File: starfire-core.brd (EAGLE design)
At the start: 60 x 52 mm, 70 parts, among them Q1 FDN340P, Y1 16MHZ

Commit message: starfire eaglecad lbr refernce moved.
I renamed and moved the EagleCAD library for the PCB fab compoment to our public git repo.  So updated the BRD and SCH references so that users can find the correct library.
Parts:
- FAB: device CircuitMonkey-solaris:PCB-BASE-B1 -> solstice-design-system:PCB-BASE-B1
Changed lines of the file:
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@@
 <attribute name="VALUE" x="-24.5" y="23" size="0.6096" layer="27" font="vector" align="center"/>
 </element>
-<element name="FAB" library="CircuitMonkey-solaris" package="PCB-BASE-B1" value="STARFIRE PCB" x="0" y="0" smashed="yes"/>
+<element name="FAB" library="solstice-design-system" package="PCB-BASE-B1" value="STARFIRE PCB" x="0" y="0" smashed="yes"/>
 <element name="OPAMP" library="Seeed-IC" package="MSOP8-0.65-3X3MM" value="LMV358IDGKR-MSOP8" x="-15" y="-3.3048" smashed="yes">
 <attribute name="MPN" value="LMV358IDGKR" x="-15" y="-3.3048" size="1.778" layer="27" display="off"/>

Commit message: Rev. A PCBs shared to world
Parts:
- removed WS1, WS10, WS11, WS12, WS13, WS14, WS15, WS16, WS2, WS3, WS4, WS5, WS6, WS7, WS8, WS9: WS2812, led:NEOPIXEL
- added C17, C18: 10uf, Seeed-Capacitor:C0603
- added SK0, SK1, SK10, SK11, SK12, SK13, SK14, SK15, SK2, SK3, SK4, SK5, SK6, SK7, SK8, SK9: SK6812-MINI, led:SMD_3535
- added UMBRA: DF12-20DS-0.5V, co-hirose:DF12-20P-RCPT-MTL-BOSS
- added US0, US1, US2: TPSMD-040-RND, con-testpoints:SMD-040MIL-RND
- RESET: value B3U-1000P-2P-SMD -> MOM (OFF)-ON; device Seeed-Switch:SW2-2.6-3.0X2.5X1.2+0.4MM -> comp-switch:SWITCH-0635-2P-SMD
- VR33: value XC6206P332MR-G-SOT23 -> 3.3V
- moved RESET 77.9 mm to (27.5, 42.6), turned to 0 degrees
- moved C8 40.7 mm to (34.5, 16.6), turned to 90 degrees
- moved C16 39.2 mm to (16.7, 23.1), turned to 270 degrees
- moved 5-12V 39.0 mm to (0.10, 34.0)
- moved USB 38.5 mm to (1.50, 24.0)
- moved C1 38.4 mm to (33.0, 31.6)
- moved C10 38.4 mm to (15.0, 28.2)
- moved C11 38.4 mm to (15.0, 26.8)
- moved C12 38.4 mm to (21.0, 22.6)
- moved C13 38.4 mm to (12.0, 36.8)
- moved C14 38.4 mm to (23.9, 34.4)
- moved C15 38.4 mm to (21.0, 18.4)
- moved C2 38.4 mm to (21.0, 25.2)
- moved C3 38.4 mm to (21.0, 19.8)
- moved C4 38.4 mm to (33.0, 30.2)
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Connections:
- removed net MOSI/WS2812: ICSP.5, R8.1, UC.10
- removed net N$29: WS11.2, WS12.4
- removed net N$30: WS12.2, WS13.4
- removed net N$31: WS13.2, WS14.4
- removed net N$32: WS14.2, WS15.4
- removed net N$33: WS15.2, WS16.4
- removed net PIXELS: R8.2, WS1.4
- removed net SCK: ICSP.2, UC.9
- new net MOSI: ICSP.5, UC.10, UMBRA.16
- new net N$1: SK0.1, SK1.3
- new net N$12: SK6.1, SK7.3
- new net N$4: SK1.1, SK2.3
- new net N$5: SK2.1, SK3.3
- new net N$6: SK3.1, SK4.3
- new net N$9: SK4.1, SK5.3
- new net SCK/PIXELS: ICSP.2, R8.1, UC.9, UMBRA.12
- new net SL0: UMBRA.2, US0.TP
- new net SL1: UMBRA.4, US1.TP
- new net SL2: UMBRA.6, US2.TP
- net !RESET: now also RESET.1, UMBRA.10; no longer RESET.2
- net +3V3: now also UMBRA.8
- net D0: now also UMBRA.15
- net D1: now also UMBRA.13
- net D2: now also UMBRA.11
- net D3: now also UMBRA.9
- net D4: now also UMBRA.7
- net D5: now also UMBRA.5
- net D6: now also UMBRA.3
- net D7: now also UMBRA.1
- net GND: now also C17.1, C18.1, HL4.1, RESET.2, SK0.2, SK1.2, SK10.2, SK11.2, SK12.2, SK13.2, SK14.2, SK15.2, SK2.2, SK3.2, SK4.2, SK5.2, SK6.2, SK7.2, SK8.2, SK9.2, UMBRA.19, UMBRA.20; no longer HL4.2, RESET.1, WS1.3, WS10.3, WS11.3, WS12.3, WS13.3, WS14.3, WS15.3, WS16.3, WS2.3, WS3.3, WS4.3, WS5.3, WS6.3, WS7.3, WS8.3, WS9.3
- net MISO: now also UMBRA.14
- net N$11: now also SK5.1, SK6.3; no longer WS1.2, WS2.4
- net N$13: now also SK8.1, SK9.3; no longer WS2.2, WS3.4
- net N$14: now also R8.2, SK0.3; no longer WS3.2, WS4.4
- net N$15: now also SK10.3, SK9.1; no longer WS4.2, WS5.4
- net N$16: now also SK10.1, SK11.3; no longer WS5.2, WS6.4
- net N$17: now also SK11.1, SK12.3; no longer WS6.2, WS7.4
- net N$18: now also SK12.1, SK13.3; no longer WS7.2, WS8.4
- net N$19: now also SK13.1, SK14.3; no longer WS8.2, WS9.4
- net N$20: now also SK14.1, SK15.3; no longer WS10.4, WS9.2
- net N$28: now also SK7.1, SK8.3; no longer WS10.2, WS11.4
- net VCC: now also C17.2, C18.2, SK0.4, SK1.4, SK10.4, SK11.4, SK12.4, SK13.4, SK14.4, SK15.4, SK2.4, SK3.4, SK4.4, SK5.4, SK6.4, SK7.4, SK8.4, SK9.4, UMBRA.17, UMBRA.18; no longer WS1.1, WS10.1, WS11.1, WS12.1, WS13.1, WS14.1, WS15.1, WS16.1, WS2.1, WS3.1, WS4.1, WS5.1, WS6.1, WS7.1, WS8.1, WS9.1
- net VIN: now also HL4.2; no longer HL4.1
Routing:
- net SCK/PIXELS: track 0.00 -> 60.3 mm, vias 0 -> 2
- net N$28: track 4.32 -> 59.0 mm, vias 0 -> 2
- net MOSI: track 0.00 -> 54.1 mm, vias 0 -> 2
- net N$19: track 53.3 -> 4.32 mm, vias 2 -> 0
- net N$14: track 4.32 -> 43.9 mm, vias 0 -> 2
- net D7: track 23.8 -> 63.3 mm
- net MOSI/WS2812: track 35.1 -> 0.00 mm, vias 2 -> 0
- net D4: track 31.0 -> 58.5 mm
- net +3V3: track 42.0 -> 69.4 mm, vias 3 -> 4
- net D6: track 29.6 -> 55.9 mm, vias 0 -> 2
- net SCK: track 25.9 -> 0.00 mm, vias 2 -> 0
- net D5: track 35.6 -> 60.5 mm
- net D3: track 32.7 -> 57.5 mm
- net D2: track 34.5 -> 58.5 mm
- net D1: track 33.6 -> 56.5 mm
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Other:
- board size 60 x 52 mm -> 60 x 48 mm
- board text added: "Rev. A"
- board text removed: "Rev. *"

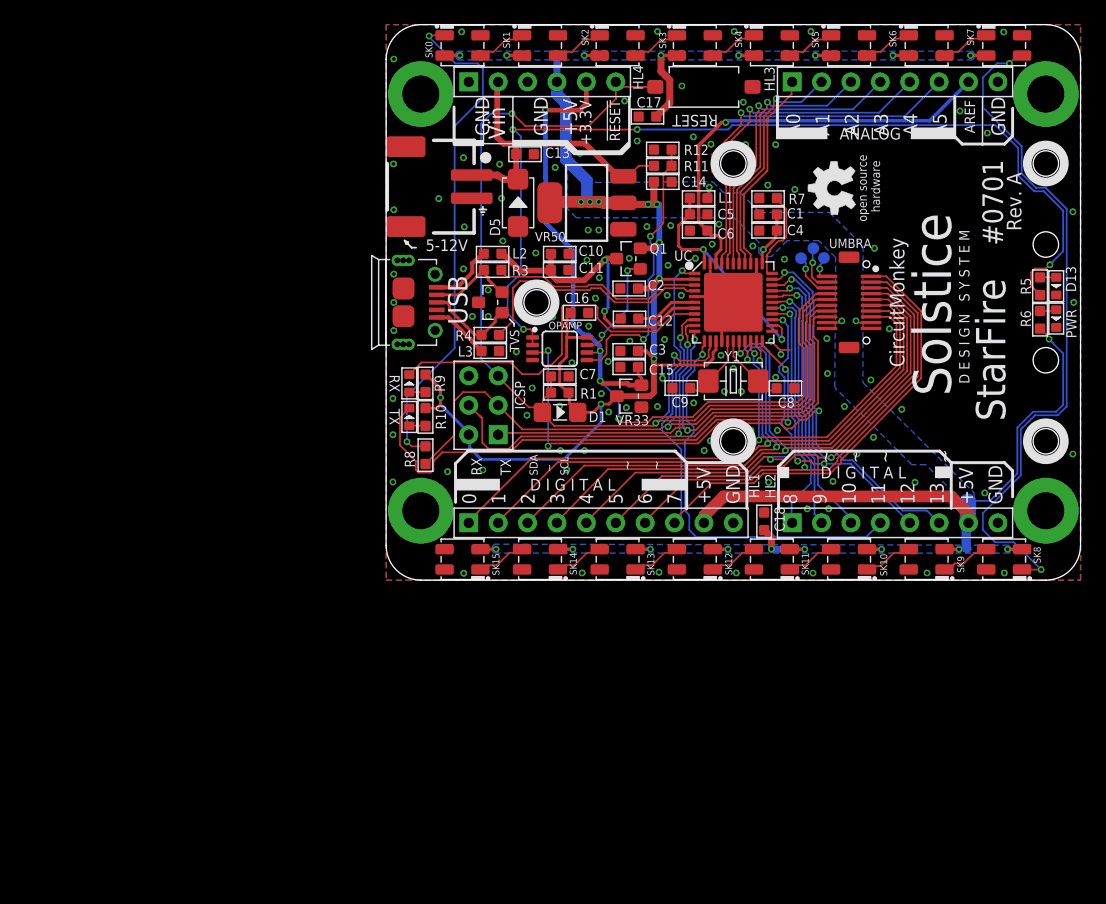
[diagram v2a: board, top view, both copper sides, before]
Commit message: Revision B released
Added Umbra connector feature along with Umbra mount support holes.  RGB LEDs are now smaller SK6812 type 3.5x3.5mm.   Added output test points for external LED chain that extends on-board chain.  Added PIXEL_EN solder jumper so that user can disable on board pixels if needed.
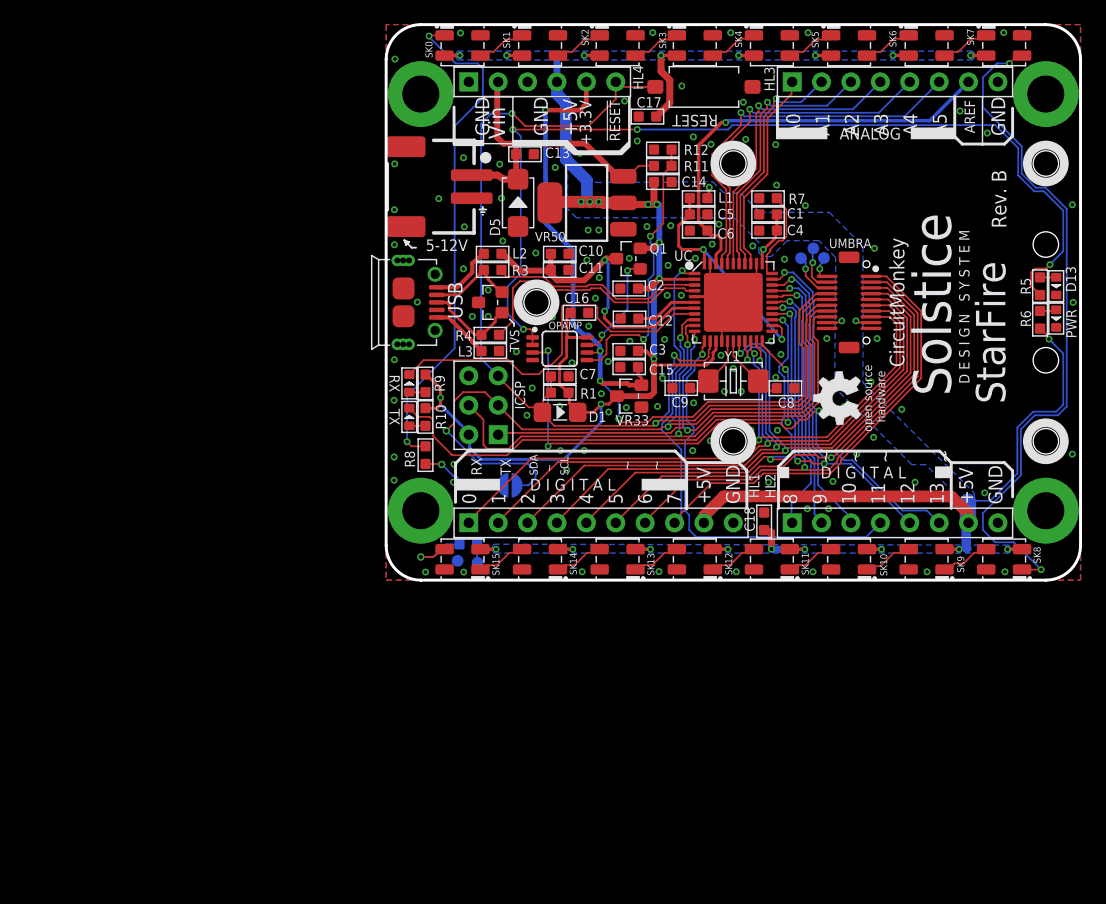
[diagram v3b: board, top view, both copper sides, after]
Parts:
- added EN_PIXELS: (no value), rlc:SOLDER_JUMP_80MIL_RND
- added PXGND, PXO: TPSMD-040-RND, con-testpoints:SMD-040MIL-RND
- added R2: 330R, Seeed-Resistor:R0603
- USB: value ZX62-B-5PA -> USB-Micro-SMT+THD
- moved U$3 43.4 mm to (47.2, 14.5)
- moved U$2 18.2 mm to (39.2, 15.7)
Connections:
- new net N$29: PXO.TP, R2.1
- new net N$30: R2.2, SK15.1
- new net PIXELS: EN_PIXELS.2, R8.1
- net GND: now also PXGND.TP
- net SCK/PIXELS: now also EN_PIXELS.1; no longer R8.1
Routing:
- net SCK/PIXELS: track 60.3 -> 68.1 mm, vias 2 -> 3
- net PIXELS: track 0.00 -> 7.37 mm, vias 0 -> 1
- net N$30: track 0.00 -> 6.12 mm, vias 0 -> 1
- net TX_LED: track 48.9 -> 44.6 mm
- net GND: track 18.2 -> 15.6 mm, vias 113 -> 114
- net N$29: track 0.00 -> 1.61 mm
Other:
- board text added: "Open Source by CircuitMonkey"
- board text added: "Rev. B"
- board text removed: "#0701"
- board text removed: "Rev. A"
